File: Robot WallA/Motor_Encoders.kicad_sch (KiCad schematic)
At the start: 6 parts, among them J26 39501-1004, J27 39501-1004

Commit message: Continued to link MCU pins, Added a sheet for servomotors and optional 2 DC motors.
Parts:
- renumbered C105 to C104, C104 to C105
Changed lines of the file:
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@@
 		(dnp no)
 		(fields_autoplaced yes)
-		(property "Reference" "#PWR0109"
+		(property "Reference" "#PWR0111"
 			(at 104.14 46.99 0)
 			(effects
@@
 			(project "PCB"
 				(path "/117fd49e-499d-4b54-b58c-f6b538ecca4a/a16960dc-56f6-4cf6-af27-6c174f94c7f8/70c9705a-afb2-475a-a6a4-6cf804f4b2b1"
-					(reference "#PWR0109")
+					(reference "#PWR0111")
 					(unit 1)
 				)
@@
 		(on_board yes)
 		(dnp no)
-		(property "Reference" "C105"
+		(property "Reference" "C104"
 			(at 113.284 39.624 90)
 			(effects
@@
 			(project "PCB"
 				(path "/117fd49e-499d-4b54-b58c-f6b538ecca4a/a16960dc-56f6-4cf6-af27-6c174f94c7f8/70c9705a-afb2-475a-a6a4-6cf804f4b2b1"
-					(reference "C105")
+					(reference "C104")
 					(unit 1)
 				)
@@
 		(dnp no)
 		(fields_autoplaced yes)
-		(property "Reference" "#PWR0107"
+		(property "Reference" "#PWR0112"
 			(at 123.19 81.28 0)
 			(effects
@@
 			(project ""
 				(path "/117fd49e-499d-4b54-b58c-f6b538ecca4a/a16960dc-56f6-4cf6-af27-6c174f94c7f8/70c9705a-afb2-475a-a6a4-6cf804f4b2b1"
-					(reference "#PWR0107")
+					(reference "#PWR0112")
 					(unit 1)
 				)
@@
 		(dnp no)
 		(fields_autoplaced yes)
-		(property "Reference" "#PWR0108"
+		(property "Reference" "#PWR0113"
 			(at 123.19 97.79 0)
 			(effects
@@
 			(project "PCB"
 				(path "/117fd49e-499d-4b54-b58c-f6b538ecca4a/a16960dc-56f6-4cf6-af27-6c174f94c7f8/70c9705a-afb2-475a-a6a4-6cf804f4b2b1"
-					(reference "#PWR0108")
+					(reference "#PWR0113")
 					(unit 1)
 				)
@@
 		(on_board yes)
 		(dnp no)
-		(property "Reference" "C104"
+		(property "Reference" "C105"
 			(at 127.254 39.624 90)
 			(effects
@@
 			(project "PCB"
 				(path "/117fd49e-499d-4b54-b58c-f6b538ecca4a/a16960dc-56f6-4cf6-af27-6c174f94c7f8/70c9705a-afb2-475a-a6a4-6cf804f4b2b1"
-					(reference "C104")
+					(reference "C105")
 					(unit 1)
 				)

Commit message: Defined every footprints
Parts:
- C101: renamed from C104; footprint CAPC2012X94N -> Capacitor_SMD:C_0603_1608Metric_Pad1.08x0.95mm_HandSolder; Arrow Part Number 0805DC104MAT2A -> (none); Arrow Price/Stock https://www.arrow.com/en/products/0805dc104mat2a/avx -> (none); Height 0.94 -> (none); Manufacturer_Name Kyocera AVX -> (none); Manufacturer_Part_Number 0805DC104MAT2A -> (none); Mouser Part Number 581-0805DC104MAT2A -> (none); Mouser Price/Stock https://www.mouser.com/Search/Refine.aspx?Keyword=581-0805D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 -> (none)
- C102: renamed from C105; footprint CAPC2012X94N -> Capacitor_SMD:C_0603_1608Metric_Pad1.08x0.95mm_HandSolder; Arrow Part Number 0805DC104MAT2A -> (none); Arrow Price/Stock https://www.arrow.com/en/products/0805dc104mat2a/avx -> (none); Height 0.94 -> (none); Manufacturer_Name Kyocera AVX -> (none); Manufacturer_Part_Number 0805DC104MAT2A -> (none); Mouser Part Number 581-0805DC104MAT2A -> (none); Mouser Price/Stock https://www.mouser.com/Search/Refine.aspx?Keyword=581-0805D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 -> (none)
- C103: renamed from C106; footprint CAPC2012X94N -> Capacitor_SMD:C_0603_1608Metric_Pad1.08x0.95mm_HandSolder; Arrow Part Number 0805DC104MAT2A -> (none); Arrow Price/Stock https://www.arrow.com/en/products/0805dc104mat2a/avx -> (none); Height 0.94 -> (none); Manufacturer_Name Kyocera AVX -> (none); Manufacturer_Part_Number 0805DC104MAT2A -> (none); Mouser Part Number 581-0805DC104MAT2A -> (none); Mouser Price/Stock https://www.mouser.com/Search/Refine.aspx?Keyword=581-0805D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 -> (none)
- C104: renamed from C107; footprint CAPC2012X94N -> Capacitor_SMD:C_0603_1608Metric_Pad1.08x0.95mm_HandSolder; Arrow Part Number 0805DC104MAT2A -> (none); Arrow Price/Stock https://www.arrow.com/en/products/0805dc104mat2a/avx -> (none); Height 0.94 -> (none); Manufacturer_Name Kyocera AVX -> (none); Manufacturer_Part_Number 0805DC104MAT2A -> (none); Mouser Part Number 581-0805DC104MAT2A -> (none); Mouser Price/Stock https://www.mouser.com/Search/Refine.aspx?Keyword=581-0805D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 -> (none)
- J15: renamed from J26; footprint 395011004 -> SamacSys_Parts:395011004; Height 9.6 -> (none); Manufacturer_Name Molex -> (none); Mouser Part Number 538-39501-1004 -> (none); Mouser Price/Stock https://www.mouser.co.uk/ProductDetail/Molex/39501-1004?qs=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 -> (none)
- J16: renamed from J27; footprint 395011004 -> SamacSys_Parts:395011004; Height 9.6 -> (none); Manufacturer_Name Molex -> (none); Mouser Part Number 538-39501-1004 -> (none); Mouser Price/Stock https://www.mouser.co.uk/ProductDetail/Molex/39501-1004?qs=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 -> (none)

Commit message: Updated USB UART converter, Linked telemeter sensors.
Updated components indicators
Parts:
- renumbered J15 to J17, J16 to J18
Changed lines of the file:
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@@
 		(dnp no)
 		(fields_autoplaced yes)
-		(property "Reference" "J15"
+		(property "Reference" "J17"
 			(at 146.05 76.1999 0)
 			(effects
@@
 			(project ""
 				(path "/117fd49e-499d-4b54-b58c-f6b538ecca4a/a16960dc-56f6-4cf6-af27-6c174f94c7f8/70c9705a-afb2-475a-a6a4-6cf804f4b2b1"
-					(reference "J15")
+					(reference "J17")
 					(unit 1)
 				)
@@
 		(dnp no)
 		(fields_autoplaced yes)
-		(property "Reference" "#PWR0102"
+		(property "Reference" "#PWR0107"
 			(at 104.14 46.99 0)
 			(effects
@@
 			(project "PCB"
 				(path "/117fd49e-499d-4b54-b58c-f6b538ecca4a/a16960dc-56f6-4cf6-af27-6c174f94c7f8/70c9705a-afb2-475a-a6a4-6cf804f4b2b1"
-					(reference "#PWR0102")
+					(reference "#PWR0107")
 					(unit 1)
 				)
@@
 		(dnp no)
 		(fields_autoplaced yes)
-		(property "Reference" "#PWR0103"
+		(property "Reference" "#PWR0108"
 			(at 123.19 81.28 0)
 			(effects
@@
 			(project ""
 				(path "/117fd49e-499d-4b54-b58c-f6b538ecca4a/a16960dc-56f6-4cf6-af27-6c174f94c7f8/70c9705a-afb2-475a-a6a4-6cf804f4b2b1"
-					(reference "#PWR0103")
+					(reference "#PWR0108")
 					(unit 1)
 				)
@@
 		(dnp no)
 		(fields_autoplaced yes)
-		(property "Reference" "#PWR0104"
+		(property "Reference" "#PWR0109"
 			(at 123.19 97.79 0)
 			(effects
@@
 			(project "PCB"
 				(path "/117fd49e-499d-4b54-b58c-f6b538ecca4a/a16960dc-56f6-4cf6-af27-6c174f94c7f8/70c9705a-afb2-475a-a6a4-6cf804f4b2b1"
-					(reference "#PWR0104")
+					(reference "#PWR0109")
 					(unit 1)
 				)
@@
 		(dnp no)
 		(fields_autoplaced yes)
-		(property "Reference" "J16"
+		(property "Reference" "J18"
 			(at 146.05 92.7099 0)
 			(effects
@@
 			(project "PCB"
 				(path "/117fd49e-499d-4b54-b58c-f6b538ecca4a/a16960dc-56f6-4cf6-af27-6c174f94c7f8/70c9705a-afb2-475a-a6a4-6cf804f4b2b1"
-					(reference "J16")
-					(unit 1)
-				)
+					(reference "J18")
+					(unit 1)
+				)

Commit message: Conitnue routing
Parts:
- renumbered J18 to J17, J17 to J18
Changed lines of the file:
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@@
+	(wire
+		(pts
+			(xy 44.45 29.21) (xy 36.83 29.21)
+		)
+		(stroke
+			(width 0)
+			(type default)
+		)
+	)
 	(wire
 		(pts
@@
 	(wire
 		(pts
+			(xy 44.45 36.83) (xy 36.83 36.83)
+		)
+		(stroke
+			(width 0)
+			(type default)
+		)
+	)
+	(wire
+		(pts
 			(xy 119.38 46.99) (xy 133.35 46.99)
 		)
@@
 	(wire
 		(pts
+			(xy 44.45 34.29) (xy 36.83 34.29)
+		)
+		(stroke
+			(width 0)
+			(type default)
+		)
+	)
+	(wire
+		(pts
 			(xy 38.1 25.4) (xy 44.45 25.4)
 		)
@@
 			(width 0)
 			(type default)
+		)
+	)
+	(wire
+		(pts
+			(xy 44.45 31.75) (xy 36.83 31.75)
+		)
+		(stroke
+			(width 0)
+			(type default)
+		)
+	)
+	(label "ENCODER_RIGHT_1"
+		(at 44.45 34.29 0)
+		(effects
+			(font
+				(size 1.27 1.27)
+			)
+			(justify left bottom)
+		)
+	)
+	(label "ENCODER_RIGHT_2"
+		(at 129.54 95.25 180)
+		(effects
+			(font
+				(size 1.27 1.27)
+			)
+			(justify right bottom)
 		)
 	)
@@
 		)
 	)
+	(label "ENCODER_RIGHT_2"
+		(at 44.45 36.83 0)
+		(effects
+			(font
+				(size 1.27 1.27)
+			)
+			(justify left bottom)
+		)
+	)
 	(label "5V"
 		(at 44.45 25.4 0)
@@
 		)
 	)
+	(label "ENCODER_LEFT_1"
+		(at 129.54 76.2 180)
+		(effects
+			(font
+				(size 1.27 1.27)
+			)
+			(justify right bottom)
+		)
+	)
+	(label "ENCODER_RIGHT_1"
+		(at 129.54 92.71 180)
+		(effects
+			(font
+				(size 1.27 1.27)
+			)
+			(justify right bottom)
+		)
+	)
 	(label "5V"
 		(at 129.54 73.66 180)
@@
 		)
 	)
+	(label "ENCODER_LEFT_2"
+		(at 129.54 78.74 180)
+		(effects
+			(font
+				(size 1.27 1.27)
+			)
+			(justify right bottom)
+		)
+	)
 	(label "5V"
 		(at 129.54 90.17 180)
@@
 		)
 	)
-	(hierarchical_label "ENCODER_LEFT_2"
-		(shape input)
-		(at 129.54 78.74 180)
+	(label "ENCODER_LEFT_2"
+		(at 44.45 31.75 0)
+		(effects
+			(font
+				(size 1.27 1.27)
+			)
+			(justify left bottom)
+		)
+	)
+	(label "ENCODER_LEFT_1"
+		(at 44.45 29.21 0)
+		(effects
+			(font
+				(size 1.27 1.27)
+			)
+			(justify left bottom)
+		)
+	)
+	(hierarchical_label "ENCODER_RIGHT_2"
+		(shape output)
+		(at 36.83 36.83 180)
 		(effects
 			(font
@@
 		)
 	)
-	(hierarchical_label "ENCODER_RIGHT_2"
-		(shape input)
-		(at 129.54 95.25 180)
+	(hierarchical_label "ENCODER_RIGHT_1"
+		(shape output)
+		(at 36.83 34.29 180)
+		(effects
+			(font
+				(size 1.27 1.27)
+			)
+			(justify right)
+		)
+	)
+	(hierarchical_label "ENCODER_LEFT_1"
+		(shape output)
+		(at 36.83 29.21 180)
 		(effects
 			(font
@@
 		)
 	)
-	(hierarchical_label "ENCODER_RIGHT_1"
-		(shape input)
-		(at 129.54 92.71 180)
-		(effects
-			(font
-				(size 1.27 1.27)
-			)
-			(justify right)
-		)
-	)
-	(hierarchical_label "ENCODER_LEFT_1"
-		(shape input)
-		(at 129.54 76.2 180)
+	(hierarchical_label "ENCODER_LEFT_2"
+		(shape output)
+		(at 36.83 31.75 180)
 		(effects
 			(font
@@
 		(dnp no)
 		(fields_autoplaced yes)
-		(property "Reference" "J17"
+		(property "Reference" "J18"
 			(at 146.05 76.1999 0)
 			(effects
@@
 			(project ""
 				(path "/117fd49e-499d-4b54-b58c-f6b538ecca4a/a16960dc-56f6-4cf6-af27-6c174f94c7f8/70c9705a-afb2-475a-a6a4-6cf804f4b2b1"
-					(reference "J17")
+					(reference "J18")
 					(unit 1)
 				)
@@
 		(dnp no)
 		(fields_autoplaced yes)
-		(property "Reference" "J18"
+		(property "Reference" "J17"
 			(at 146.05 92.7099 0)
 			(effects
@@
 			(project "PCB"
 				(path "/117fd49e-499d-4b54-b58c-f6b538ecca4a/a16960dc-56f6-4cf6-af27-6c174f94c7f8/70c9705a-afb2-475a-a6a4-6cf804f4b2b1"
-					(reference "J18")
+					(reference "J17")
 					(unit 1)
 				)

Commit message: Updated fab files.
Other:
- company: (none) -> Socotec Monitoring
- title: (none) -> Robot Wall-A
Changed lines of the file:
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@@
 	(generator_version "9.0")
 	(paper "A4")
+	(title_block
+		(title "Robot Wall-A")
+		(date "2025-09-20")
+		(rev "v1.0")
+		(company "Socotec Monitoring")
+		(comment 1 "GDU")
+		(comment 2 "THO")
+	)
 	(junction
 		(at 133.35 46.99)
@@
 			)
 		)
+		(property "MPN" ""
+			(at 129.54 73.66 0)
+			(effects
+				(font
+					(size 1.27 1.27)
+				)
+				(hide yes)
+			)
+		)
 		(pin "2"
 		)
@@
 				)
 				(justify left top)
+				(hide yes)
+			)
+		)
+		(property "MPN" ""
+			(at 146.05 34.29 90)
+			(effects
+				(font
+					(size 1.27 1.27)
+				)
 				(hide yes)
 			)
@@
 			)
 		)
+		(property "MPN" ""
+			(at 119.38 34.29 90)
+			(effects
+				(font
+					(size 1.27 1.27)
+				)
+				(hide yes)
+			)
+		)
 		(pin "2"
 		)
@@
 				)
 				(justify left top)
+				(hide yes)
+			)
+		)
+		(property "MPN" ""
+			(at 158.75 34.29 90)
+			(effects
+				(font
+					(size 1.27 1.27)
+				)
 				(hide yes)
 			)
@@
 			)
 		)
+		(property "MPN" ""
+			(at 133.35 34.29 90)
+			(effects
+				(font
+					(size 1.27 1.27)
+				)
+				(hide yes)
+			)
+		)
 		(pin "2"
 		)
@@
 				(hide yes)
 			)
+		)
+		(property "MPN" ""
+			(at 129.54 90.17 0)
+			(effects
+				(font
+					(size 1.27 1.27)
+				)
+				(hide yes)
+			)

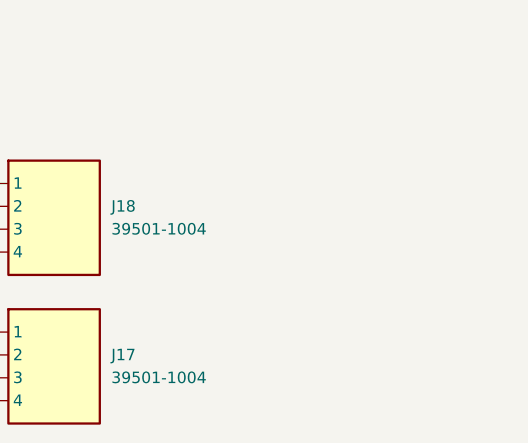
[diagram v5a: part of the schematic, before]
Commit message: Added to BOM connectors and socket
Updated fab files
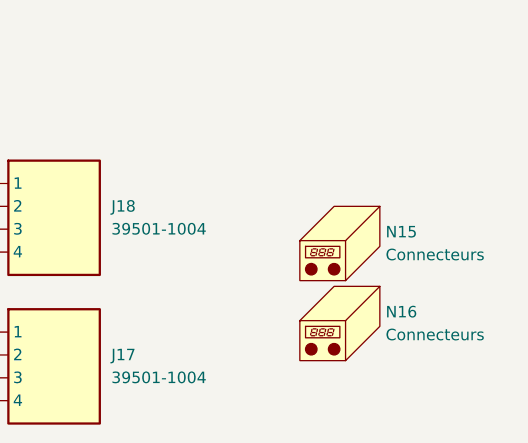
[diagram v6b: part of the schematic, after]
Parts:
- added N15, N16: Connecteurs, symbol Mechanical:Housing
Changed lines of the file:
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@@
-			)
-		)
-		(property "MPN" ""
-			(at 129.54 73.66 0)
-			(effects
-				(font
-					(size 1.27 1.27)
-				)
-				(hide yes)
 			)
 		)
@@
 				)
 				(justify left top)
-				(hide yes)
-			)
-		)
-		(property "MPN" ""
-			(at 146.05 34.29 90)
-			(effects
-				(font
-					(size 1.27 1.27)
-				)
 				(hide yes)
 			)
@@
 			)
 		)
-		(property "MPN" ""
-			(at 119.38 34.29 90)
-			(effects
-				(font
-					(size 1.27 1.27)
-				)
-				(hide yes)
-			)
-		)
 		(pin "2"
 		)
@@
 				)
 				(justify left top)
-				(hide yes)
-			)
-		)
-		(property "MPN" ""
-			(at 158.75 34.29 90)
-			(effects
-				(font
-					(size 1.27 1.27)
-				)
 				(hide yes)
 			)
@@
 	)
 	(symbol
+		(lib_id "Mechanical:Housing")
+		(at 172.72 88.9 0)
+		(unit 1)
+		(exclude_from_sim no)
+		(in_bom yes)
+		(on_board no)
+		(dnp no)
+		(property "Reference" "N16"
+			(at 176.53 87.9474 0)
+			(effects
+				(font
+					(size 1.27 1.27)
+				)
+				(justify left)
+			)
+		)
+		(property "Value" "Connecteurs"
+			(at 176.53 90.4874 0)
+			(effects
+				(font
+					(size 1.27 1.27)
+				)
+				(justify left)
+			)
+		)
+		(property "Footprint" ""
+			(at 173.99 87.63 0)
+			(effects
+				(font
+					(size 1.27 1.27)
+				)
+				(hide yes)
+			)
+		)
+		(property "Datasheet" "~"
+			(at 173.99 87.63 0)
+			(effects
+				(font
+					(size 1.27 1.27)
+				)
+				(hide yes)
+			)
+		)
+		(property "Description" "Housing"
+			(at 172.72 88.9 0)
+			(effects
+				(font
+					(size 1.27 1.27)
+				)
+				(hide yes)
+			)
+		)
+		(property "Manufacturer_Part_Number" "39503-2004"
+			(at 172.72 88.9 0)
+			(effects
+				(font
+					(size 1.27 1.27)
+				)
+				(hide yes)
+			)
+		)
+		(instances
+			(project "Robot WallA"
+				(path "/117fd49e-499d-4b54-b58c-f6b538ecca4a/a16960dc-56f6-4cf6-af27-6c174f94c7f8/70c9705a-afb2-475a-a6a4-6cf804f4b2b1"
+					(reference "N16")
+					(unit 1)
+				)
+			)
+		)
+	)
+	(symbol
 		(lib_id "SamacSys_Parts:0805DC104MAT2A")
 		(at 133.35 34.29 270)
@@
 			)
 		)
-		(property "MPN" ""
-			(at 133.35 34.29 90)
-			(effects
-				(font
-					(size 1.27 1.27)
-				)
-				(hide yes)
-			)
-		)
 		(pin "2"
 		)
@@
 				(path "/117fd49e-499d-4b54-b58c-f6b538ecca4a/a16960dc-56f6-4cf6-af27-6c174f94c7f8/70c9705a-afb2-475a-a6a4-6cf804f4b2b1"
 					(reference "C102")
+					(unit 1)
+				)
+			)
+		)
+	)
+	(symbol
+		(lib_id "Mechanical:Housing")
+		(at 172.72 80.01 0)
+		(unit 1)
+		(exclude_from_sim no)
+		(in_bom yes)
+		(on_board no)
+		(dnp no)
+		(property "Reference" "N15"
+			(at 176.53 79.0574 0)
+			(effects
+				(font
+					(size 1.27 1.27)
+				)
+				(justify left)
+			)
+		)
+		(property "Value" "Connecteurs"
+			(at 176.53 81.5974 0)
+			(effects
+				(font
+					(size 1.27 1.27)
+				)
+				(justify left)
+			)
+		)
+		(property "Footprint" ""
+			(at 173.99 78.74 0)
+			(effects
+				(font
+					(size 1.27 1.27)
+				)
+				(hide yes)
+			)
+		)
+		(property "Datasheet" "~"
+			(at 173.99 78.74 0)
+			(effects
+				(font
+					(size 1.27 1.27)
+				)
+				(hide yes)
+			)
+		)
+		(property "Description" "Housing"
+			(at 172.72 80.01 0)
+			(effects
+				(font
+					(size 1.27 1.27)
+				)
+				(hide yes)
+			)
+		)
+		(property "Manufacturer_Part_Number" "39503-2004"
+			(at 172.72 80.01 0)
+			(effects
+				(font
+					(size 1.27 1.27)
+				)
+				(hide yes)
+			)
+		)
+		(instances
+			(project "Robot WallA"
+				(path "/117fd49e-499d-4b54-b58c-f6b538ecca4a/a16960dc-56f6-4cf6-af27-6c174f94c7f8/70c9705a-afb2-475a-a6a4-6cf804f4b2b1"
+					(reference "N15")
 					(unit 1)
 				)
@@
 				(hide yes)
 			)
-		)
-		(property "MPN" ""
-			(at 129.54 90.17 0)
-			(effects
-				(font
-					(size 1.27 1.27)
-				)
-				(hide yes)
-			)

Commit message: Modified footprint to simplify BOM. Finalized BOM.
Updated fab files
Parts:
- C101, C102: Manufacturer_Part_Number (none) -> CL10A106MA8NRNC
- C103, C104: Manufacturer_Part_Number (none) -> KGM15BR71H104KT
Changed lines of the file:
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@@
+			)
+		)
+		(property "Arrow Part Number" ""
+			(at 129.54 73.66 0)
+			(effects
+				(font
+					(size 1.27 1.27)
+				)
+				(hide yes)
+			)
+		)
+		(property "Arrow Price/Stock" ""
+			(at 129.54 73.66 0)
+			(effects
+				(font
+					(size 1.27 1.27)
+				)
+				(hide yes)
+			)
+		)
+		(property "Mouser Price/Stock" ""
+			(at 129.54 73.66 0)
+			(effects
+				(font
+					(size 1.27 1.27)
+				)
+				(hide yes)
 			)
 		)
@@
 			)
 		)
-		(property "Manufacturer_Part_Number" ""
+		(property "Manufacturer_Part_Number" "KGM15BR71H104KT "
 			(at -450.14 43.18 0)
 			(effects
@@
 				)
 				(justify left top)
+				(hide yes)
+			)
+		)
+		(property "Arrow Part Number" ""
+			(at 146.05 34.29 90)
+			(effects
+				(font
+					(size 1.27 1.27)
+				)
+				(hide yes)
+			)
+		)
+		(property "Arrow Price/Stock" ""
+			(at 146.05 34.29 90)
+			(effects
+				(font
+					(size 1.27 1.27)
+				)
+				(hide yes)
+			)
+		)
+		(property "Mouser Price/Stock" ""
+			(at 146.05 34.29 90)
+			(effects
+				(font
+					(size 1.27 1.27)
+				)
 				(hide yes)
 			)
@@
 			)
 		)
-		(property "Manufacturer_Part_Number" ""
+		(property "Manufacturer_Part_Number" "CL10A106MA8NRNC"
 			(at -476.81 43.18 0)
 			(effects
@@
 				)
 				(justify left top)
+				(hide yes)
+			)
+		)
+		(property "Arrow Part Number" ""
+			(at 119.38 34.29 90)
+			(effects
+				(font
+					(size 1.27 1.27)
+				)
+				(hide yes)
+			)
+		)
+		(property "Arrow Price/Stock" ""
+			(at 119.38 34.29 90)
+			(effects
+				(font
+					(size 1.27 1.27)
+				)
+				(hide yes)
+			)
+		)
+		(property "Mouser Price/Stock" ""
+			(at 119.38 34.29 90)
+			(effects
+				(font
+					(size 1.27 1.27)
+				)
 				(hide yes)
 			)
@@
 			)
 		)
-		(property "Manufacturer_Part_Number" ""
+		(property "Manufacturer_Part_Number" "KGM15BR71H104KT "
 			(at -437.44 43.18 0)
 			(effects
@@
 				)
 				(justify left top)
+				(hide yes)
+			)
+		)
+		(property "Arrow Part Number" ""
+			(at 158.75 34.29 90)
+			(effects
+				(font
+					(size 1.27 1.27)
+				)
+				(hide yes)
+			)
+		)
+		(property "Arrow Price/Stock" ""
+			(at 158.75 34.29 90)
+			(effects
+				(font
+					(size 1.27 1.27)
+				)
+				(hide yes)
+			)
+		)
+		(property "Mouser Price/Stock" ""
+			(at 158.75 34.29 90)
+			(effects
+				(font
+					(size 1.27 1.27)
+				)
 				(hide yes)
 			)
@@
 			)
 		)
+		(property "Arrow Part Number" ""
+			(at 172.72 88.9 0)
+			(effects
+				(font
+					(size 1.27 1.27)
+				)
+				(hide yes)
+			)
+		)
+		(property "Arrow Price/Stock" ""
+			(at 172.72 88.9 0)
+			(effects
+				(font
+					(size 1.27 1.27)
+				)
+				(hide yes)
+			)
+		)
+		(property "Mouser Price/Stock" ""
+			(at 172.72 88.9 0)
+			(effects
+				(font
+					(size 1.27 1.27)
+				)
+				(hide yes)
+			)
+		)
 		(instances
 			(project "Robot WallA"
@@
 			)
 		)
-		(property "Manufacturer_Part_Number" ""
+		(property "Manufacturer_Part_Number" "CL10A106MA8NRNC"
 			(at -462.84 43.18 0)
 			(effects
@@
 				)
 				(justify left top)
+				(hide yes)
+			)
+		)
+		(property "Arrow Part Number" ""
+			(at 133.35 34.29 90)
+			(effects
+				(font
+					(size 1.27 1.27)
+				)
+				(hide yes)
+			)
+		)
+		(property "Arrow Price/Stock" ""
+			(at 133.35 34.29 90)
+			(effects
+				(font
+					(size 1.27 1.27)
+				)
+				(hide yes)
+			)
+		)
+		(property "Mouser Price/Stock" ""
+			(at 133.35 34.29 90)
+			(effects
+				(font
+					(size 1.27 1.27)
+				)
 				(hide yes)
 			)
@@
 		)
 		(property "Manufacturer_Part_Number" "39503-2004"
+			(at 172.72 80.01 0)
+			(effects
+				(font
+					(size 1.27 1.27)
+				)
+				(hide yes)
+			)
+		)
+		(property "Arrow Part Number" ""
+			(at 172.72 80.01 0)
+			(effects
+				(font
+					(size 1.27 1.27)
+				)
+				(hide yes)
+			)
+		)
+		(property "Arrow Price/Stock" ""
+			(at 172.72 80.01 0)
+			(effects
+				(font
+					(size 1.27 1.27)
+				)
+				(hide yes)
+			)
+		)
+		(property "Mouser Price/Stock" ""
 			(at 172.72 80.01 0)
 			(effects
@@
 				(hide yes)
 			)
+		)
+		(property "Arrow Part Number" ""
+			(at 129.54 90.17 0)
+			(effects
+				(font
+					(size 1.27 1.27)
+				)
+				(hide yes)
+			)
+		)
+		(property "Arrow Price/Stock" ""
+			(at 129.54 90.17 0)
+			(effects
+				(font
+					(size 1.27 1.27)
+				)
+				(hide yes)
+			)
+		)
+		(property "Mouser Price/Stock" ""
+			(at 129.54 90.17 0)
+			(effects
+				(font
+					(size 1.27 1.27)
+				)
+				(hide yes)
+			)

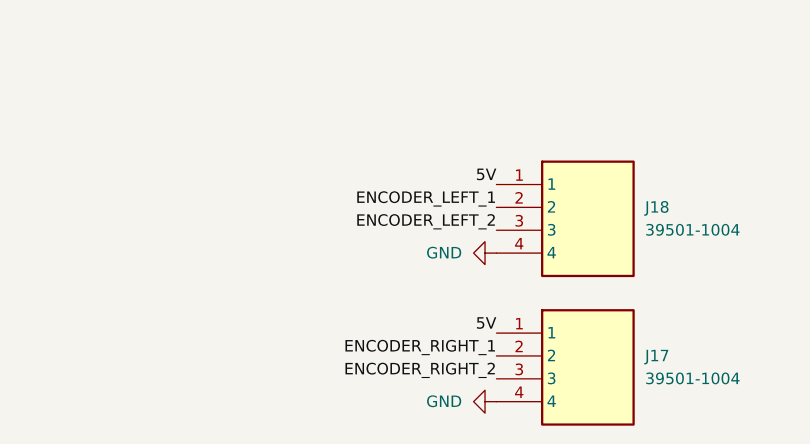
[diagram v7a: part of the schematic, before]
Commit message: Corrected schematic labels encoders according to PCB labels... (inversion...)
Add fab files
cleaned
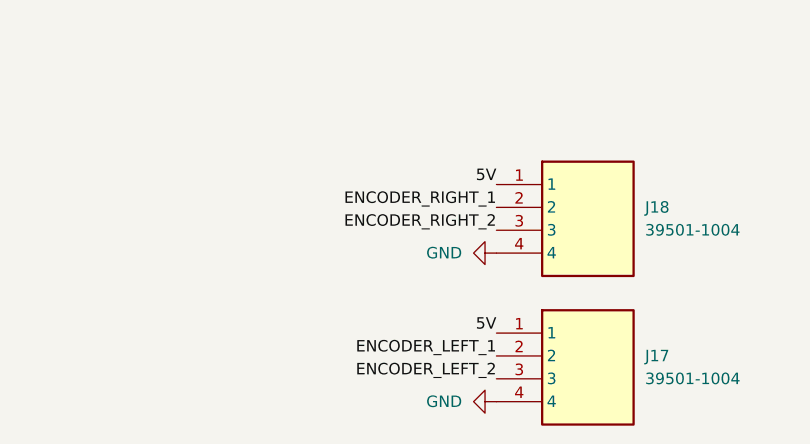
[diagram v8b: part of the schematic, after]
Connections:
- net ENCODER_LEFT_1: now also J17.2; no longer J18.2
- net ENCODER_LEFT_2: now also J17.3; no longer J18.3
- net ENCODER_RIGHT_1: now also J18.2; no longer J17.2
- net ENCODER_RIGHT_2: now also J18.3; no longer J17.3
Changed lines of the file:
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@@
 	)
 	(label "ENCODER_RIGHT_2"
-		(at 129.54 95.25 180)
+		(at 129.54 78.74 180)
 		(effects
 			(font
@@
 	)
 	(label "ENCODER_LEFT_1"
-		(at 129.54 76.2 180)
+		(at 129.54 92.71 180)
 		(effects
 			(font
@@
 	)
 	(label "ENCODER_RIGHT_1"
-		(at 129.54 92.71 180)
+		(at 129.54 76.2 180)
 		(effects
 			(font
@@
 	)
 	(label "ENCODER_LEFT_2"
-		(at 129.54 78.74 180)
+		(at 129.54 95.25 180)
 		(effects
 			(font
